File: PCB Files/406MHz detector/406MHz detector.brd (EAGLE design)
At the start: 177.8 x 96.5 mm, 66 parts, among them IC1 FT232RL, J1 power switch, J2 pwr_input, J3 select jumper, J4 select jumper, J5 reset switch, U2 ATMEGA328P_TQFP, Y1 8MHz

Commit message: ensuring updates are pushed
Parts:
- removed JP7: card detect, SparkFun-Jumpers:SMT-JUMPER_2_NO_SILK
- removed U$1: USB-B, capstone:USB
- removed U$3: CSRM100, capstone:CSRM
- removed U$5: DIODE, capstone:SMA-DIODE
- removed U$7: A32270-ND, capstone:A33270-ND
- added C21: 0.1uF, SparkFun-Capacitors:0603
- added C22: TBD, SparkFun-Capacitors:0603
- added D2: 3A/40V/500mV, SparkFun-DiscreteSemi:SMA-DIODE
- added FB1, FB2, FB3, FB4, FB5, FB6: (no value), capstone:0603
- added J10: SMA, capstone:SMA_R/A
- added J7, J8: select jumper, SparkFun-Connectors:1X03_LOCK
- added JP5: JUMPER-SMT_3_2-NC_TRACE_SILK, SparkFun-Jumpers:SMT-JUMPER_3_2-NC_TRACE_SILK
- added U4: ATMEGA328P_TQFP, SparkFun-IC-Microcontroller:TQFP32-08
- C10: value 1mf -> 10.0uF; device SparkFun-Capacitors:CPOL-RADIAL-5MM-10MM-KIT -> SparkFun-Capacitors:1206
- C11: value 10uF -> 0.1uF; device SparkFun-Capacitors:1206 -> SparkFun-Capacitors:0805
- C12: value 10uF -> 10.0uF
- C13, C7: device SparkFun-Capacitors:0805 -> SparkFun-Capacitors:0603
- C15, C16: value 0.1uF -> 10uF; device SparkFun-Capacitors:0603 -> SparkFun-Capacitors:1206
- C19: value TBD -> 0.1uF
- C2: value 10nF -> 0.1uF; device SparkFun-Capacitors:0603 -> SparkFun-Capacitors:0805
- C3: value 22uF -> 1mf; device SparkFun-Capacitors:0805 -> SparkFun-Capacitors:CPOL-RADIAL-5MM-10MM-KIT
- C4, C5: value 10.0uF -> 1mf; device SparkFun-Capacitors:1206 -> SparkFun-Capacitors:CPOL-RADIAL-5MM-10MM-KIT
- C6: value TBD -> 10nF
- C8: value 1mf -> 22uF; device SparkFun-Capacitors:CPOL-RADIAL-5MM-10MM-KIT -> SparkFun-Capacitors:0805
- C9: value 1mf -> TBD; device SparkFun-Capacitors:CPOL-RADIAL-5MM-10MM-KIT -> SparkFun-Capacitors:0603
- D1: value 3A/40V/500mV -> DIODE; device SparkFun-DiscreteSemi:SMA-DIODE -> capstone:SMA-DIODE
- J1: value power switch -> pwr_input; device SparkFun-Connectors:1X02 -> SparkFun-Connectors:1X02_LOCK
- J2: value pwr_input -> power switch; device SparkFun-Connectors:1X02_LOCK -> SparkFun-Connectors:1X02
- J3: value select jumper -> (none); device SparkFun-Connectors:1X03_LOCK -> SparkFun-Connectors:1X02
- J4: value select jumper -> USB-B; device SparkFun-Connectors:1X03_LOCK -> capstone:USB
- J6: value (none) -> A32270-ND; device SparkFun-Connectors:1X02 -> capstone:A33270-ND
- JP6: value JUMPER-SMT_3_2-NC_TRACE_SILK -> card detect; device SparkFun-Jumpers:SMT-JUMPER_3_2-NC_TRACE_SILK -> SparkFun-Jumpers:SMT-JUMPER_2_NO_SILK
- L2, L3: value TBD -> 68µH/±20%/1.05A; device SparkFun-Coils:0603 -> SparkFun-Coils:CR75
- L5, L6: value 68µH/±20%/1.05A -> TBD; device SparkFun-Coils:CR75 -> SparkFun-Coils:0603
- R1: value 100K -> 100
- R2: value 26.7k -> 100; device SparkFun-Resistors:0603 -> SparkFun-Resistors:0402
- R6: value 100 -> 100K
- R7: value 100 -> 26.7k; device SparkFun-Resistors:0402 -> SparkFun-Resistors:0603
- U2: value ATMEGA328P_TQFP -> CSRM100; device SparkFun-IC-Microcontroller:TQFP32-08 -> capstone:CSRM
- moved L6 157.9 mm to (162.3, 72.9), turned to 270 degrees
- moved L3 154.4 mm to (10.2, 30.5), turned to 90 degrees
- moved J6 153.5 mm to (167.9, 78.5), turned to 0 degrees
- moved L5 146.6 mm to (152.9, 72.9), turned to 270 degrees
- moved C9 141.7 mm to (157.7, 73.9), turned to 180 degrees
- moved L2 141.5 mm to (10.2, 39.4), turned to 90 degrees
- moved C6 137.3 mm to (24.1, 19.1), turned to 0 degrees
- moved U2 105.1 mm to (145.8, 60.2), turned to 180 degrees
- moved C18 96.1 mm to (14.0, 74.9), turned to 180 degrees
- moved J3 85.4 mm to (30.5, 10.2), turned to 90 degrees
- moved R6 82.2 mm to (14.7, 15.7)
- moved R7 78.1 mm to (14.7, 19.3)
- moved JP4 76.4 mm to (141.2, 47.5)
- moved C3 76.3 mm to (22.9, 54.6), turned to 270 degrees
- moved C14 76.0 mm to (33.3, 55.6), turned to 90 degrees
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- renumbered U$2 to U1, U$4 to U3, U$6 to U5, U$8 to J9
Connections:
- removed net N$25: U5.P$11
- removed net N$26: U5.P$10
- new net INTERNAL_3.3V: C15.1, IC1.17, IC1.4
- new net N$20: C18.1, FB3.1, IC1.20
- new net N$29: C19.1, C21.1, FB4.2, FB6.1, R11.2, U5.P$5
- new net N$30: C7.1, FB1.2, U2.PWR_IN
- new net N$31: C17.1, FB2.2, U4.18, U4.20, U4.4, U4.6
- new net N$45: C20.1, FB5.2, J9.P4
- net !CSRM_LED_SINK: now also U2.LED; no longer U$3.LED
- net 3.3V: now also C12.1, C13.1, FB1.1, FB2.1, FB4.1, FB5.1; no longer C14.1, C15.1, C17.1, C18.1, C20.1, C5.1, IC1.17, IC1.4, J9.P4, R11.2, U$3.PWR_IN, U2.18, U2.20, U2.4, U2.6, U5.P$5
- net 5V: now also C10.1, C8.1, L4.P$2, R6.2; no longer C3.1, C4.1, L1.P$2, R1.2
- net AC_PWR: now also D1.A, J1.2; no longer J2.2, U$5.A
- net ANTENNA_CONNECTOR: now also C9.1, J6.OUT, L6.1; no longer C6.1, L3.1, U$7.OUT
- net BOOT: now also C6.1; no longer C2.1
- net CSRM_EN: now also R4.1; no longer R8.1
- net CSRM_GPIO1: now also U2.GPIO1; no longer U$3.GPIO1
- net CSRM_GPIO2: now also U2.GPIO2; no longer U$3.GPIO2
- net CSRM_GPIO3: now also U2.GPIO3; no longer U$3.GPIO3
- net CSRM_OSC_OUT: now also U2.OSC_OUT; no longer U$3.OSC_OUT
- net CSRM_PPS: now also R8.2, U4.12; no longer R3.2, U2.12
- net CSRM_RESET: now also JP5.1, U2._RESET; no longer JP6.1, U$3._RESET
- net CSRM_RX: now also J8.2, JP2.1, R2.1; no longer J4.2, JP3.1, R6.1
- net CSRM_TX: now also J7.2, JP3.1, R3.1; no longer J3.2, JP4.1, R7.1
- net EJECT_SD: now also J3.2; no longer J6.2
- net FB: now also R6.1, R7.2; no longer R1.1, R2.2
- net GND: now also C10.2, C11.2, C12.2, C14.1, C16.1, C19.2, C2.2, C21.2, C3.-, C4.-, C5.-, C8.2, D2.A, J10.P$2, J10.P$3, J10.P$4, J10.P$5, J3.1, J4.4, J4.S1, J4.S2, J6.GND1, J6.GND2, J6.GND3, J6.GND4, L5.2, L6.2, R7.1, U2.GND, U2.GND1, U2.GND2, U2.GND3, U2.GND4, U4.21, U4.3, U4.5; no longer C10.-, C11.1, C12.1, C14.2, C16.2, C3.2, C4.2, C5.2, C8.-, C9.-, D1.A, J6.1, L2.2, L3.2, R2.1, U$1.4, U$1.S1, U$1.S2, U$3.GND, U$3.GND1, U$3.GND2, U$3.GND3, U$3.GND4, U$7.GND1, U$7.GND2, U$7.GND3, U$7.GND4, U2.21, U2.3, U2.5
- net GPS_ANTENNA: now also C22.2; no longer C19.2
- net GPS_CONNECTOR: now also C22.1, FB6.2, J10.P$1; no longer C19.1
- net GPS_SERIAL_IN: now also JP1.1, R1.1, U5.P$10; no longer JP2.1, R5.1
- net GPS_SERIAL_OUT: now also JP4.1, R5.1, U5.P$11; no longer JP1.1, R4.1
- net HF_SWITCH: now also C6.2, D2.C, L4.P$1; no longer C2.2, D1.C, L1.P$1
- net MISO: now also U4.16; no longer U2.16
- net MOSI: now also U4.15; no longer U2.15
- net N$1: now also JP4.2, R5.2, U2.TX1; no longer JP1.2, R4.2, U$3.TX1
- net N$13: now also JP6.1; no longer JP7.1
- net N$15: now also D1.C, L1.P$1; no longer L4.P$1, U$5.C
- net N$16: now also C3.+, L1.P$2, L2.P$1; no longer C8.+, L4.P$2, L5.P$1
- net N$17: now also C4.+, L2.P$2, L3.P$1; no longer C9.+, L5.P$2, L6.P$1
- net N$2: now also C2.1, J2.2; no longer C7.1, J1.2
- net N$21: now also C14.2, U4.7; no longer C12.2, U2.7
- net N$22: now also C16.2, U4.8; no longer C11.2, U2.8
- net N$27: now also U4.10; no longer U2.10
- net N$3: now also R8.1, U2.PPS; no longer R3.1, U$3.PPS
- net N$4: now also JP1.2, R1.2, U2.RX1; no longer JP2.2, R5.2, U$3.RX1
- net N$5: now also JP2.2, R2.2, U2.RX2; no longer JP3.2, R6.2, U$3.RX2
- net N$6: now also JP3.2, R3.2, U2.TX2; no longer JP4.2, R7.2, U$3.TX2
- net N$7: now also C9.2, L5.1, U2.406_IN; no longer C6.2, L2.1, U$3.406_IN
- net N$8: now also R4.2, U2.EN; no longer R8.2, U$3.EN
- net RESET: now also C11.1, JP5.2; no longer C13.1, JP6.2
- net SCLK: now also U4.17; no longer U2.17
- net SD_CD: now also JP6.2, U4.11; no longer JP7.2, U2.11
- net SS: now also U4.14; no longer U2.14
- net UC_RESET: now also JP5.3, U4.29; no longer JP6.3, R10.1, U2.29
- net UC_RX: now also J7.1, U4.30; no longer J3.1, U2.30
- net UC_TX: now also J8.1, U4.31; no longer J4.1, U2.31
- net USB_DM: now also J4.2; no longer U$1.2
- net USB_DP: now also J4.3; no longer U$1.3
- net USB_RX: now also J7.3; no longer J3.3
- net USB_TX: now also J8.3; no longer J4.3
- net USB_VCC: now also FB3.2, J4.1; no longer C16.1, IC1.20, U$1.1
- net VIN: now also C5.+, L3.P$2; no longer C10.+, L6.P$2
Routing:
- net N$5: track 0.00 -> 28.1 mm
- net N$6: track 0.00 -> 25.1 mm
- net N$1: track 0.00 -> 23.4 mm
- net N$4: track 0.00 -> 19.4 mm
- net N$3: track 0.00 -> 12.9 mm, vias 0 -> 1
- net INTERNAL_3.3V: track 0.00 -> 10.6 mm
- net 3.3V: track 10.4 -> 0.00 mm
- net N$20: track 0.00 -> 6.75 mm
- net GPS_SERIAL_OUT: track 0.00 -> 4.83 mm
- net CSRM_TX: track 0.00 -> 4.01 mm
- net GPS_SERIAL_IN: track 0.00 -> 4.01 mm
- net USB_VCC: track 9.08 -> 5.49 mm
- net USB_DP: track 9.49 -> 10.8 mm
- net USB_DM: track 7.22 -> 8.58 mm

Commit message: latest update of schematic, sent to kevin for double check
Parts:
- removed R10: 100K, SparkFun-Resistors:0402
- added C23: 0.1uF, SparkFun-Capacitors:0603
- J3: value (none) -> eject sd card
- R11: value 100K -> 10K
- moved JP5 18.8 mm to (31.5, 67.1)
- moved C21 18.2 mm to (163.6, 16.0), turned to 180 degrees
- moved JP6 16.6 mm to (32.0, 76.7), turned to 180 degrees
- moved FB6 11.9 mm to (164.6, 19.3), turned to 90 degrees
- moved C15 8.65 mm to (23.6, 66.0), turned to 270 degrees
- moved L5 3.10 mm to (155.4, 74.7)
- moved C9 2.34 mm to (158.2, 76.2)
- moved R9 2.30 mm to (33.5, 72.4)
- moved L6 2.18 mm to (161.0, 74.7)
- moved J6 1.05 mm to (167.6, 79.5)
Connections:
- removed net N$19: U5.P$9
- removed net N$23: U5.P$4
- removed net N$27: U4.10
- removed net N$9: IC1.19, R10.2
- net CSRM_EN: now also U4.9
- net EJECT_SD: now also U4.2
- net GND: now also IC1.11, IC1.26, U5.P$9
- net GPS_ENABLE: now also U4.10
- net GPS_SERIAL_IN: now also U4.1
- net N$10: now also C23.1, IC1.2; no longer IC1.23
- net UC_RESET: now also C23.2, U5.P$4
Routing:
- net UC_RESET: track 0.00 -> 27.6 mm, vias 0 -> 2
- net MOSI: track 0.00 -> 25.4 mm, vias 0 -> 2
- net MISO: track 0.00 -> 20.9 mm
- net SCLK: track 0.00 -> 19.7 mm, vias 0 -> 2
- net SD_CD: track 0.00 -> 19.5 mm, vias 0 -> 2
- net N$45: track 0.00 -> 13.8 mm, vias 0 -> 2
- net N$13: track 0.00 -> 13.6 mm
- net ANTENNA_CONNECTOR: track 0.00 -> 11.8 mm
- net N$7: track 0.00 -> 11.6 mm
- net INTERNAL_3.3V: track 10.6 -> 18.2 mm
- net 3.3V: track 0.00 -> 2.54 mm

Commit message: library changes, schematic changes, board changes
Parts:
- removed FB1: (no value), capstone:0603
- added J11: pwr select, SparkFun-Connectors:1X03_LOCK
- added R10: 10k, SparkFun-Resistors:0603
- J1: value pwr_input -> pwr input
- moved C23 66.8 mm to (19.1, 62.5)
- moved C14 35.5 mm to (68.1, 48.8)
- moved C16 35.0 mm to (87.4, 48.8)
- moved Y1 34.8 mm to (77.7, 50.3)
- moved JP5 34.6 mm to (65.3, 59.7)
- moved C17 34.6 mm to (83.1, 64.3)
- moved FB2 34.6 mm to (82.8, 57.9)
- moved R9 34.6 mm to (67.3, 65.0)
- moved U4 34.6 mm to (74.9, 62.2)
- moved R12 25.5 mm to (29.0, 75.9)
- moved C10 7.64 mm to (45.7, 34.5)
- moved C1 7.64 mm to (28.2, 11.4)
- moved C4 7.64 mm to (23.4, 22.9)
- moved C6 7.64 mm to (24.6, 11.4)
- moved D1 7.64 mm to (39.9, 22.9)
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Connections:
- removed net N$24: U5.P$14
- removed net N$3: R8.1, U2.PPS
- removed net N$30: C7.1, FB1.2, U2.PWR_IN
- new net 5V_IN: C10.1, J11.2, U3.3
- new net GPS_PPS: R8.2, U5.P$14
- net 3.3V: now also C7.1, R10.2, U2.PWR_IN; no longer FB1.1
- net 5V: now also J11.1; no longer C10.1, U3.3
- net CSRM_PPS: now also R8.1, U2.PPS; no longer R8.2
- net N$13: no longer J9.P2
- net N$8: now also R10.1
- net SS: now also J9.P2
- net USB_VCC: now also J11.3
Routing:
- net SS: track 0.00 -> 71.4 mm
- net SD_CD: track 19.5 -> 59.8 mm
- net MOSI: track 25.4 -> 62.4 mm
- net MISO: track 20.9 -> 57.3 mm, vias 0 -> 2
- net SCLK: track 19.7 -> 54.6 mm
- net 3.3V: track 2.54 -> 29.6 mm, vias 0 -> 2
- net USB_RX: track 23.2 -> 0.00 mm, vias 1 -> 0
- net UC_RESET: track 27.6 -> 10.5 mm, vias 2 -> 1
- net N$22: track 0.00 -> 15.0 mm
- net N$21: track 0.00 -> 14.2 mm
- net N$3: track 12.9 -> 0.00 mm, vias 1 -> 0
- net CSRM_PPS: track 0.00 -> 12.9 mm, vias 0 -> 1
- net N$13: track 13.6 -> 5.43 mm
- net N$10: track 0.00 -> 7.89 mm
- net USB_TX: track 20.6 -> 13.6 mm
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
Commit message: final version of PCB to review
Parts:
- added C24: 0.1uF, SparkFun-Capacitors:0603
- added J12, J13: select jumper, SparkFun-Connectors:1X03_LOCK
- C11, C2, C8: device SparkFun-Capacitors:0805 -> SparkFun-Capacitors:0603
- R1, R2, R3, R4, R5, R8: device SparkFun-Resistors:0402 -> SparkFun-Resistors:0603
- R11: value 10K -> 10k; device SparkFun-Resistors:0402 -> SparkFun-Resistors:0603
- R6: value 100K -> 100k; device SparkFun-Resistors:0402 -> SparkFun-Resistors:0603
- moved R6 43.3 mm to (57.1, 19.1), turned to 180 degrees
- moved R7 43.0 mm to (57.1, 21.1), turned to 180 degrees
- moved C3 42.3 mm to (10.9, 6.60), turned to 90 degrees
- moved R1 40.8 mm to (109.5, 70.6), turned to 180 degrees
- moved J3 40.1 mm to (71.1, 3.56)
- moved L4 39.5 mm to (46.5, 32.8)
- moved U1 38.4 mm to (55.4, 25.4), turned to 180 degrees
- moved J1 35.3 mm to (28.4, 29.7), turned to 270 degrees
- moved C8 35.2 mm to (57.1, 17.0), turned to 180 degrees
- moved C1 33.2 mm to (56.4, 29.0)
- moved J8 31.7 mm to (89.7, 83.3)
- moved R4 31.2 mm to (132.8, 51.8), turned to 180 degrees
- moved C6 30.6 mm to (52.1, 24.9), turned to 90 degrees
- moved C5 30.5 mm to (36.1, 6.60), turned to 90 degrees
- moved C2 29.5 mm to (48.8, 4.83), turned to 270 degrees
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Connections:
- net N$2 renamed SUPPLY_ENABLE
- net N$7 renamed 406_IN
- new net LINK_1: J12.1, J8.1
- new net LINK_2: J13.1, J7.1
- new net N$2: U4.27
- new net N$3: U4.28
- new net SOFT_SERIAL_RX: J7.3, U4.25
- new net SOFT_SERIAL_TX: J8.3, U4.24
- net 5V: now also R6.1; no longer R6.2
- net CSRM_EN: now also R1.2; no longer R4.1
- net CSRM_PPS: now also R8.2; no longer R8.1
- net CSRM_RX: now also R4.2; no longer R2.1
- net CSRM_TX: now also R5.2; no longer R3.1
- net EJECT_SD: now also C24.1
- net FB: now also R6.2; no longer R6.1
- net GND: now also C24.2
- net GPS_PPS: now also R8.1; no longer R8.2
- net GPS_SERIAL_IN: now also R3.2; no longer R1.1
- net GPS_SERIAL_OUT: now also R2.2; no longer R5.1
- net N$1: now also R2.1; no longer R5.2
- net N$4: now also R3.1; no longer R1.2
- net N$5: now also R4.1; no longer R2.2
- net N$6: now also R5.1; no longer R3.2
- net N$8: now also R1.1; no longer R4.2
- net UC_RX: now also J12.3; no longer J7.1
- net UC_TX: now also J13.3; no longer J8.1
- net USB_RX: now also J13.2; no longer J7.3
- net USB_TX: now also J12.2; no longer J8.3
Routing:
- net 3.3V: track 29.6 -> 260.2 mm, vias 2 -> 5
- net UC_RESET: track 10.5 -> 176.7 mm, vias 1 -> 4
- net CSRM_RESET: track 0.00 -> 111.2 mm, vias 0 -> 1
- net GPS_SERIAL_IN: track 2.93 -> 105.2 mm, vias 0 -> 4
- net USB_RX: track 0.00 -> 102.1 mm, vias 0 -> 6
- net CSRM_PPS: track 12.9 -> 113.7 mm
- net GPS_ENABLE: track 0.00 -> 83.9 mm, vias 0 -> 2
- net CSRM_TX: track 3.29 -> 83.6 mm, vias 0 -> 1
- net EJECT_SD: track 0.00 -> 73.7 mm, vias 0 -> 4
- net N$29: track 0.00 -> 70.1 mm, vias 0 -> 2
- net 5V: track 0.00 -> 67.6 mm
- net CSRM_RX: track 0.00 -> 66.4 mm, vias 0 -> 1
- net RESET: track 0.00 -> 66.0 mm, vias 0 -> 2
- net USB_TX: track 13.6 -> 79.4 mm, vias 1 -> 4
- net GND: track 0.00 -> 54.6 mm, vias 3 -> 71
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- added copper zone on layer 1, net 3.3V
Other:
- board text added: "Capstone Group 16 Ellis Junker Sean Mazer Nathan McKay Connor Scott Sarah Weston"
- board text added: "USB | AC Power selection"
- board text added: "When all jumpers in lower position, FTDI is connected directly to uC. CSRM conneced to software serial."
- board text added: "When all jumpers in upper position, FTDI is connected directly to CSRM."
- board text added: "lower"
- board text added: "upper"

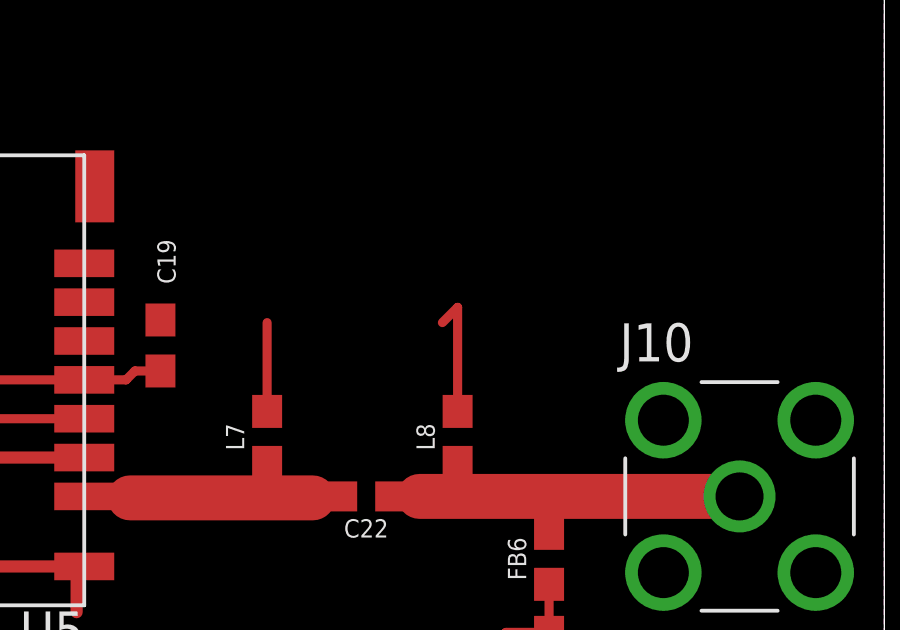
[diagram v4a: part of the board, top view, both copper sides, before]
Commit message: added arduino code
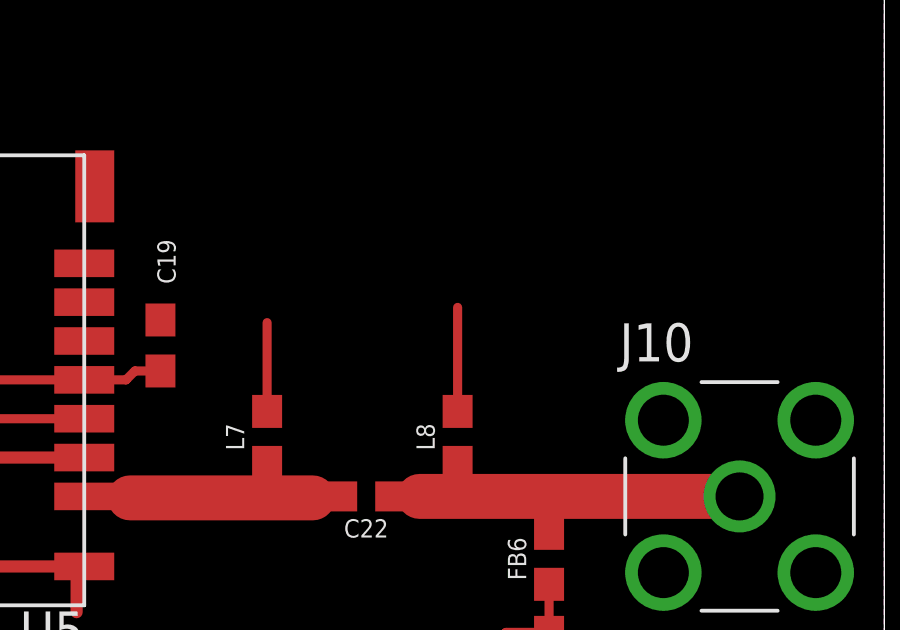
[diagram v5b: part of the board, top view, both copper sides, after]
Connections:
- removed net N$2: U4.27
- removed net N$3: U4.28
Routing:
- net GND: track 54.6 -> 53.9 mm
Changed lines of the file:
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@@
 <setting verticaltext="up"/>
 </settings>
-<grid distance="10" unitdist="mil" unit="mil" style="lines" multiple="10" display="yes" altdistance="5" altunitdist="mil" altunit="mil"/>
+<grid distance="10" unitdist="mil" unit="inch" style="lines" multiple="10" display="yes" altdistance="5" altunitdist="mil" altunit="mil"/>
 <layers>
 <layer number="1" name="Top" color="4" fill="1" visible="yes" active="yes"/>
@@
 <param name="mlMinCreamFrame" value="0mil"/>
 <param name="mlMaxCreamFrame" value="0mil"/>
-<param name="mlViaStopLimit" value="0mil"/>
+<param name="mlViaStopLimit" value="15mil"/>
 <param name="srRoundness" value="0"/>
 <param name="srMinRoundness" value="0mil"/>
@@
 <via x="137.668" y="40.386" extent="1-16" drill="0.3302"/>
 <wire x1="157.226" y1="26.504" x2="157.226" y2="29.464" width="0.3048" layer="1"/>
-<wire x1="163.068" y1="29.464" x2="163.576" y2="29.972" width="0.3048" layer="1"/>
 <wire x1="163.576" y1="26.504" x2="163.576" y2="29.972" width="0.3048" layer="1"/>
 <wire x1="151.13" y1="24.966" x2="146.378" y2="24.966" width="0.4064" layer="1"/>
@@
 <wire x1="84.074" y1="85.598" x2="84.074" y2="79.248" width="0.3048" layer="1"/>
 </signal>
-<signal name="N$2">
-<contactref element="U4" pad="27"/>
-</signal>
-<signal name="N$3">
-<contactref element="U4" pad="28"/>
-</signal>
 <signal name="LINK_1">
 <contactref element="J12" pad="1"/>
@@
 <mfgpreviewcolor name="substratecolor" color="0xFF786E46"/>
 </mfgpreviewcolors>
+<errors>
+</errors>
 </board>
 </drawing>
